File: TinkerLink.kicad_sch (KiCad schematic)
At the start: 20 parts, among them J1 Conn_01x06_Pin, Q1 IRF4905S, Q2 MMBT2222A, SW1 TS-061D-250D4-P, U1 ESP-01F-2M, U2 ME6211C33M5

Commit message: Bloody Rabbit Hole Sub-Basement!
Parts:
- USB1: value USB-212-BCW -> USB-A-USB-C; footprint LCSCfootprints:USB-A-SMD_USB-212-BCW -> tinker:USB-A-USB-C; symbol USB-A-SMD_USB-212-BCW:USB-212-BCW -> Tinker_Lib:USB-A-USB-C
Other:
- note added: "LCSCfootprints:USB-A-SMD_USB-212-BCW"
- note added: "tinker:USB_C_Hermaphrodite"
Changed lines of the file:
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@@
+		)
+	)
+	(text "LCSCfootprints:USB-A-SMD_USB-212-BCW"
+		(exclude_from_sim no)
+		(at 43.434 55.626 0)
+		(effects
+			(font
+				(size 1.27 1.27)
+			)
+		)
+	)
+	(text "tinker:USB_C_Hermaphrodite"
+		(exclude_from_sim no)
+		(at 143.51 61.468 0)
+		(effects
+			(font
+				(size 1.27 1.27)
+			)
 		)
 	)
@@
 	(wire
 		(pts
+			(xy 33.02 35.56) (xy 30.48 35.56)
+		)
+		(stroke
+			(width 0)
+			(type default)
+		)
+	)
+	(wire
+		(pts
 			(xy 87.63 57.15) (xy 87.63 58.42)
 		)
@@
 	(wire
 		(pts
-			(xy 30.48 38.1) (xy 30.48 45.72)
+			(xy 30.48 35.56) (xy 30.48 45.72)
 		)
 		(stroke
@@
 		(pts
 			(xy 172.72 25.4) (xy 172.72 39.37)
-		)
-		(stroke
-			(width 0)
-			(type default)
-		)
-	)
-	(wire
-		(pts
-			(xy 33.02 38.1) (xy 30.48 38.1)
 		)
 		(stroke
@@
 	)
 	(symbol
-		(lib_id "USB-A-SMD_USB-212-BCW:USB-212-BCW")
+		(lib_id "Tinker_Lib:USB-A-USB-C")
 		(at 43.18 39.37 0)
 		(unit 1)
@@
 			)
 		)
-		(property "Value" "USB-212-BCW"
+		(property "Value" "USB-A-USB-C"
 			(at 43.18 30.48 0)
 			(effects
@@
 			)
 		)
-		(property "Footprint" "LCSCfootprints:USB-A-SMD_USB-212-BCW"
+		(property "Footprint" "tinker:USB-A-USB-C"
 			(at 43.18 50.8 0)
 			(effects
@@
 		(pin "2"
 		)
+		(pin "B5"
+		)
+		(pin "A5"
+		)
+		(pin "B8"
+		)
+		(pin "A8"
+		)
 		(instances

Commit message: aaannnddd tweakin'...
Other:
- title: (none) -> TinkerLink
- moved on the sheet: C1, C2, C3, C4, J1, L1, LED1, R3, R4, R5, R6, SW1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

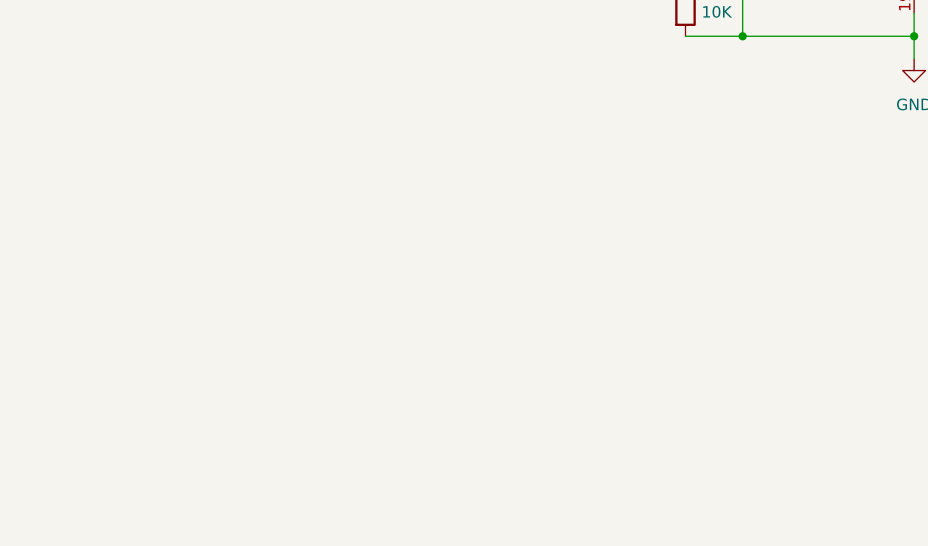
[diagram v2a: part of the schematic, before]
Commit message: Possible replacement 3v3 source
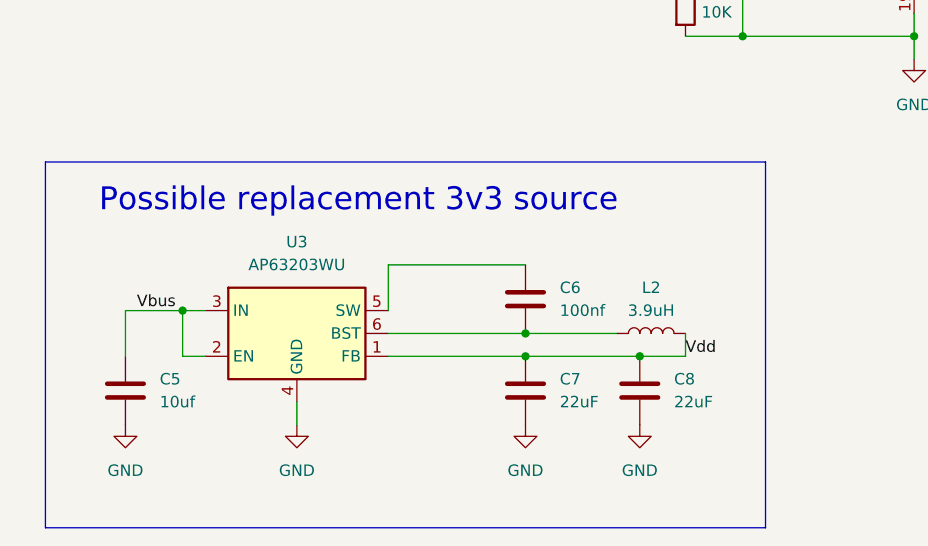
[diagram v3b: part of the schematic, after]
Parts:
- added C5: 10uf, Capacitor_SMD:C_0603_1608Metric, symbol Device:C
- added C6: 100nf, Capacitor_SMD:C_0603_1608Metric, symbol Device:C
- added C7, C8: 22uF, Capacitor_SMD:C_0603_1608Metric, symbol Device:C
- added L2: 3.9uH, Inductor_SMD:L_0603_1608Metric, symbol Device:L
- added U3: AP63203WU, Package_TO_SOT_SMD:TSOT-23-6, symbol Regulator_Switching:AP63203WU
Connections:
- net GND: now also C5.2, C7.2, C8.2, U3.4 (GND)
- net Vbus: now also C5.1, U3.2 (EN), U3.3 (IN)
- net Vdd: now also C7.1, C8.1, L2.2, U3.1 (FB)
- new net: C6.2, L2.1, U3.6 (BST)
- new net: C6.1, U3.5 (SW)
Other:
- note added: "Possible replacement 3v3 source"

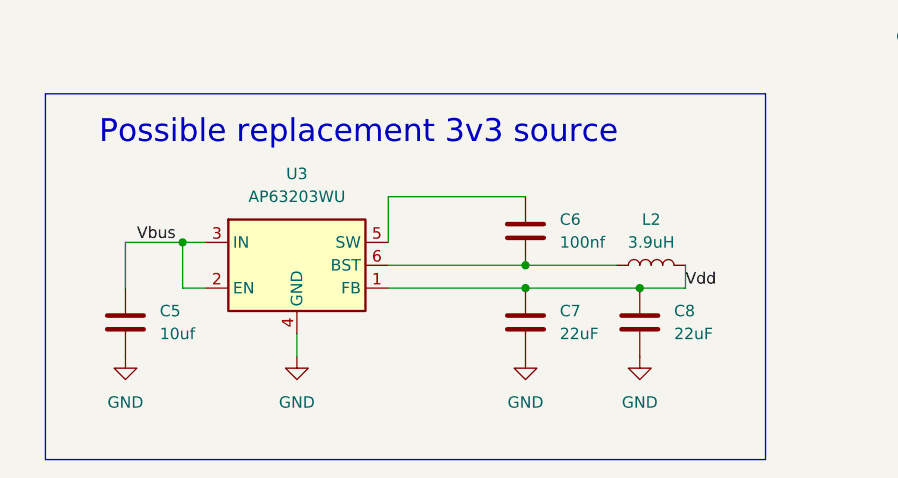
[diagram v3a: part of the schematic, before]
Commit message: Possible replacement 3v3 source
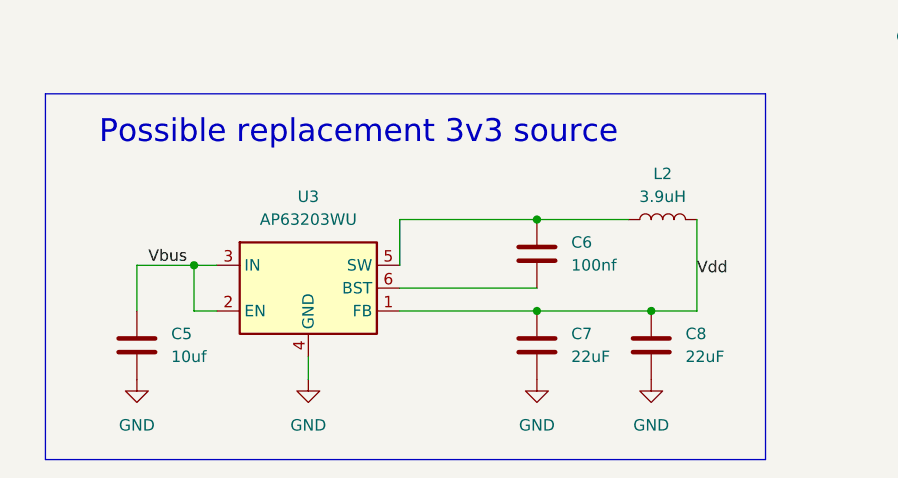
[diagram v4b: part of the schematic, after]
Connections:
- net at C6.2, U3.6 (BST): no longer L2.1
- net at C6.1, U3.5 (SW): now also L2.1
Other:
- moved on the sheet: C5, C6, C7, C8, L2, U3

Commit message: new 3v3 in place(ish)
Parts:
- added Rsh1: 0R1 1%, Resistor_SMD:R_2512_6332Metric, symbol Device:R
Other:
- note added: "Minimal 3v3 source"
- moved on the sheet: C1, C2, C3, C4, C5, C6, C7, C8, J1, L1, L2, LED1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

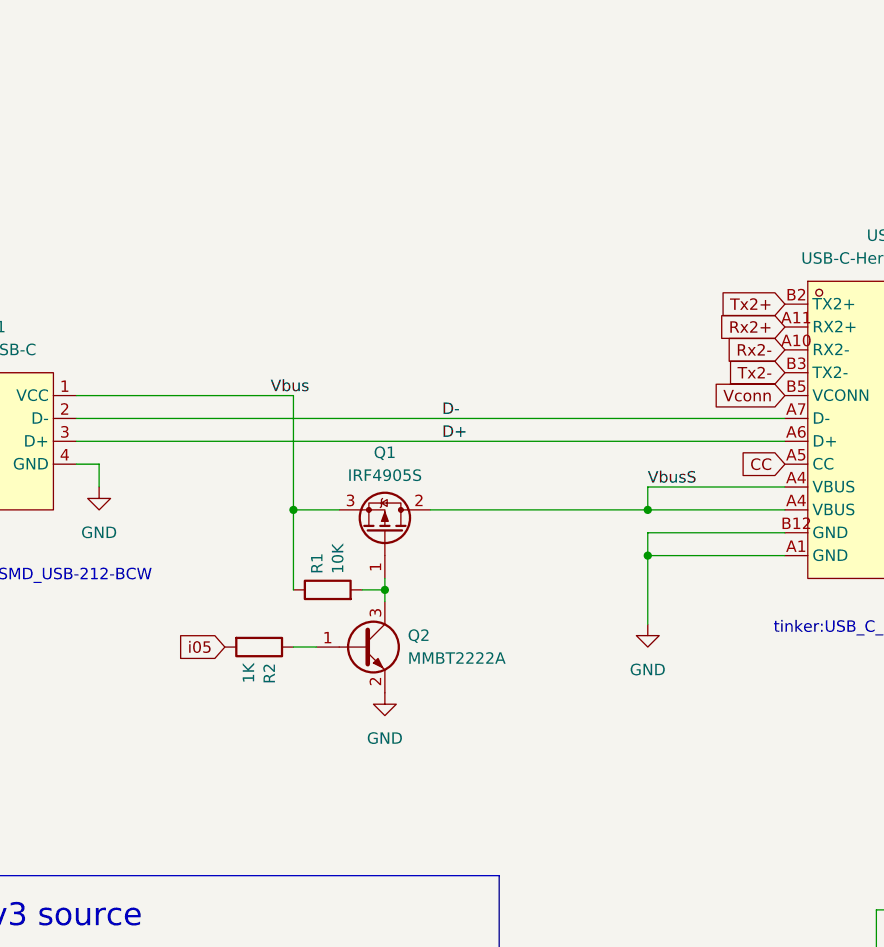
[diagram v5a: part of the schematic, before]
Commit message: Austin instigated FET change
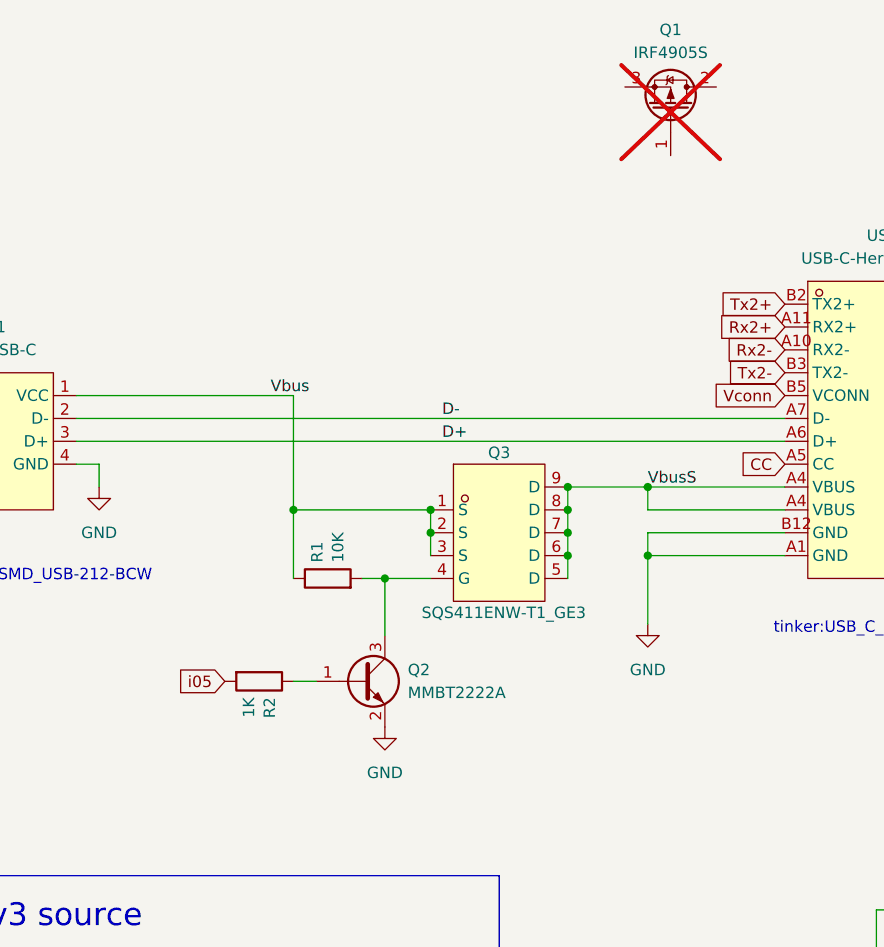
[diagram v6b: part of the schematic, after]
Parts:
- added Q3: SQS411ENW-T1_GE3, LCSCfootprints:POWERPAK-1212-8_L3.1-W3.1-P0.65-LS3.3-BL, symbol C3279469:SQS411ENW-T1_GE3
- Q1: now not fitted
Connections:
- net Vbus: now also Q3.1 (S), Q3.2 (S), Q3.3 (S); no longer Q1.3 (S)
- net VbusS: now also Q3.5 (D), Q3.6 (D), Q3.7 (D), Q3.8 (D), Q3.9 (D); no longer Q1.2 (D)
- net at Q2.3 (C), R1.2: now also Q3.4 (G); no longer Q1.1 (G)
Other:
- moved on the sheet: Q2, R1, R2

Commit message: squish...
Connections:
- net CC: now also USB1.B5
- net Rx: now also J1.3 (Pin_3); no longer J1.2 (Pin_2)
- net Tx: now also J1.4 (Pin_4); no longer J1.3 (Pin_3)
- net Vconn: now also USB1.A5
- net io0: now also J1.2 (Pin_2); no longer J1.4 (Pin_4)
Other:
- note added: "CC1 & CC2 (CC & Vconn) are interchangeable unless you need superspeed or other modes beyond USB 2. (they re swapped here...)"
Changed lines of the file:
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@@
+		)
+	)
+	(text "CC1 & CC2 (CC & Vconn) are interchangeable\nunless you need superspeed or other modes\nbeyond USB 2. (they re swapped here...)"
+		(exclude_from_sim no)
+		(at 87.376 23.114 0)
+		(effects
+			(font
+				(size 1.905 1.905)
+			)
 		)
 	)
@@
 	(wire
 		(pts
-			(xy 184.15 142.24) (xy 184.15 127)
-		)
-		(stroke
-			(width 0)
-			(type default)
-		)
-	)
-	(wire
-		(pts
 			(xy 53.34 35.56) (xy 77.47 35.56)
 		)
@@
 	(wire
 		(pts
-			(xy 189.23 134.62) (xy 189.23 142.24)
-		)
-		(stroke
-			(width 0)
-			(type default)
-		)
-	)
-	(wire
-		(pts
 			(xy 181.61 116.84) (xy 196.85 116.84)
 		)
@@
 	(wire
 		(pts
+			(xy 184.15 142.24) (xy 184.15 134.62)
+		)
+		(stroke
+			(width 0)
+			(type default)
+		)
+	)
+	(wire
+		(pts
 			(xy 59.69 165.1) (xy 74.93 165.1)
 		)
@@
 	(wire
 		(pts
-			(xy 33.02 35.56) (xy 30.48 35.56)
+			(xy 33.02 35.56) (xy 19.05 35.56)
 		)
 		(stroke
@@
 	(wire
 		(pts
+			(xy 189.23 142.24) (xy 189.23 124.46)
+		)
+		(stroke
+			(width 0)
+			(type default)
+		)
+	)
+	(wire
+		(pts
 			(xy 87.63 167.64) (xy 92.71 167.64)
 		)
@@
 	(wire
 		(pts
-			(xy 30.48 35.56) (xy 30.48 45.72)
+			(xy 19.05 35.56) (xy 19.05 46.99)
 		)
 		(stroke
@@
 	(wire
 		(pts
-			(xy 167.64 134.62) (xy 189.23 134.62)
-		)
-		(stroke
-			(width 0)
-			(type default)
-		)
-	)
-	(wire
-		(pts
 			(xy 87.63 55.88) (xy 92.71 55.88)
 		)
@@
 	(wire
 		(pts
+			(xy 184.15 134.62) (xy 167.64 134.62)
+		)
+		(stroke
+			(width 0)
+			(type default)
+		)
+	)
+	(wire
+		(pts
 			(xy 39.37 167.64) (xy 36.83 167.64)
 		)
@@
 	(wire
 		(pts
+			(xy 186.69 142.24) (xy 186.69 127)
+		)
+		(stroke
+			(width 0)
+			(type default)
+		)
+	)
+	(wire
+		(pts
 			(xy 257.81 143.51) (xy 257.81 138.43)
 		)
@@
 	(wire
 		(pts
-			(xy 186.69 124.46) (xy 167.64 124.46)
+			(xy 167.64 124.46) (xy 189.23 124.46)
 		)
 		(stroke
@@
 	(wire
 		(pts
-			(xy 184.15 127) (xy 167.64 127)
+			(xy 167.64 127) (xy 186.69 127)
 		)
 		(stroke
@@
 		(pts
 			(xy 173.99 129.54) (xy 167.64 129.54)
-		)
-		(stroke
-			(width 0)
-			(type default)
-		)
-	)
-	(wire
-		(pts
-			(xy 186.69 142.24) (xy 186.69 124.46)
 		)
 		(stroke
@@
 		)
 	)
+	(global_label "CC"
+		(shape input)
+		(at 33.02 44.45 180)
+		(fields_autoplaced yes)
+		(effects
+			(font
+				(size 1.27 1.27)
+			)
+			(justify right)
+		)
+		(property "Intersheetrefs" "${INTERSHEET_REFS}"
+			(at 27.4948 44.45 0)
+			(effects
+				(font
+					(size 1.27 1.27)
+				)
+				(justify right)
+				(hide yes)
+			)
+		)
+	)
 	(global_label "Tx2-"
 		(shape input)
@@
 		(property "Intersheetrefs" "${INTERSHEET_REFS}"
 			(at 119.842 127 0)
+			(effects
+				(font
+					(size 1.27 1.27)
+				)
+				(justify right)
+				(hide yes)
+			)
+		)
+	)
+	(global_label "Vconn"
+		(shape input)
+		(at 33.02 39.37 180)
+		(fields_autoplaced yes)
+		(effects
+			(font
+				(size 1.27 1.27)
+			)
+			(justify right)
+		)
+		(property "Intersheetrefs" "${INTERSHEET_REFS}"
+			(at 24.4106 39.37 0)
 			(effects
 				(font
@@
 	(symbol
 		(lib_id "power:GND")
-		(at 30.48 45.72 0)
+		(at 19.05 46.99 0)
 		(unit 1)
 		(exclude_from_sim no)
@@
 		(fields_autoplaced yes)
 		(property "Reference" "#PWR02"
-			(at 30.48 52.07 0)
+			(at 19.05 53.34 0)
 			(effects
 				(font
@@
 		)
 		(property "Value" "GND"
-			(at 30.48 50.8 0)
+			(at 19.05 52.07 0)
 			(effects
 				(font
@@
 		)
 		(property "Footprint" ""
-			(at 30.48 45.72 0)
+			(at 19.05 46.99 0)
 			(effects
 				(font
@@
 		)
 		(property "Datasheet" ""
-			(at 30.48 45.72 0)
+			(at 19.05 46.99 0)
 			(effects
 				(font
@@
 		)
 		(property "Description" "Power symbol creates a global label with name \"GND\" , ground"
-			(at 30.48 45.72 0)
-			(effects
-				(font
+			(at 19.05 46.99 0)
+			(effects
+				(font

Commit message: Dual FETs
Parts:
- removed Q1: IRF4905S, Package_TO_SOT_SMD:TO-252-2, symbol Transistor_FET:IRF4905
- added Q4: SQS411ENW-T1_GE3, LCSCfootprints:POWERPAK-1212-8_L3.1-W3.1-P0.65-LS3.3-BL, symbol C3279469:SQS411ENW-T1_GE3
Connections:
- net VbusS: now also Q4.1 (S), Q4.2 (S), Q4.3 (S); no longer Q3.5 (D), Q3.6 (D), Q3.7 (D), Q3.8 (D), Q3.9 (D)
- net at Q2.3 (C), Q3.4 (G), R1.2: now also Q4.4 (G)
- new net: Q3.5 (D), Q3.6 (D), Q3.7 (D), Q3.8 (D), Q3.9 (D), Q4.5 (D), Q4.6 (D), Q4.7 (D), Q4.8 (D), Q4.9 (D)
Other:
- note added: "CC1 & CC2 (CC & Vconn) are interchangeable unless you need superspeed or other modes beyond USB 2. USB-PD doesn't care. (they re swapped here...)"
- note removed: "CC1 & CC2 (CC & Vconn) are interchangeable unless you need superspeed or other modes beyond USB 2. (they re swapped here...)"
- moved on the sheet: Q2, R2, USB2
